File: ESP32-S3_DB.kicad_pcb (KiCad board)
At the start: 2 copper layers, 151 parts, among them CN1 JST_Battery, IC1 SP3071EEN-L/TR, IC2 ATA6561-GAQW-N, J1 TYPE-C-31-M12_13, J10 Conn_01x16_Socket, J11 CAN_TX, J12 CAN_RX, J2 A - B, J3 H - L, J4 TYPE-C-31-M12_13, J5 EXT_LOAD, J6 R4_TX, J7 R4_RX, J8 Micro_SD_Card_Det1, J9 Conn_01x16_Socket, Q1 NMOS, Q2 NMOS, SW1 RESET, SW2 BOOT, SW3 ON/OFF, U1 ESP32-S3FH4R2, U3 IP5306, U4 CH340X, U5 LD1117DT33CTR, X1 32.768KHz, Y1 40MHz

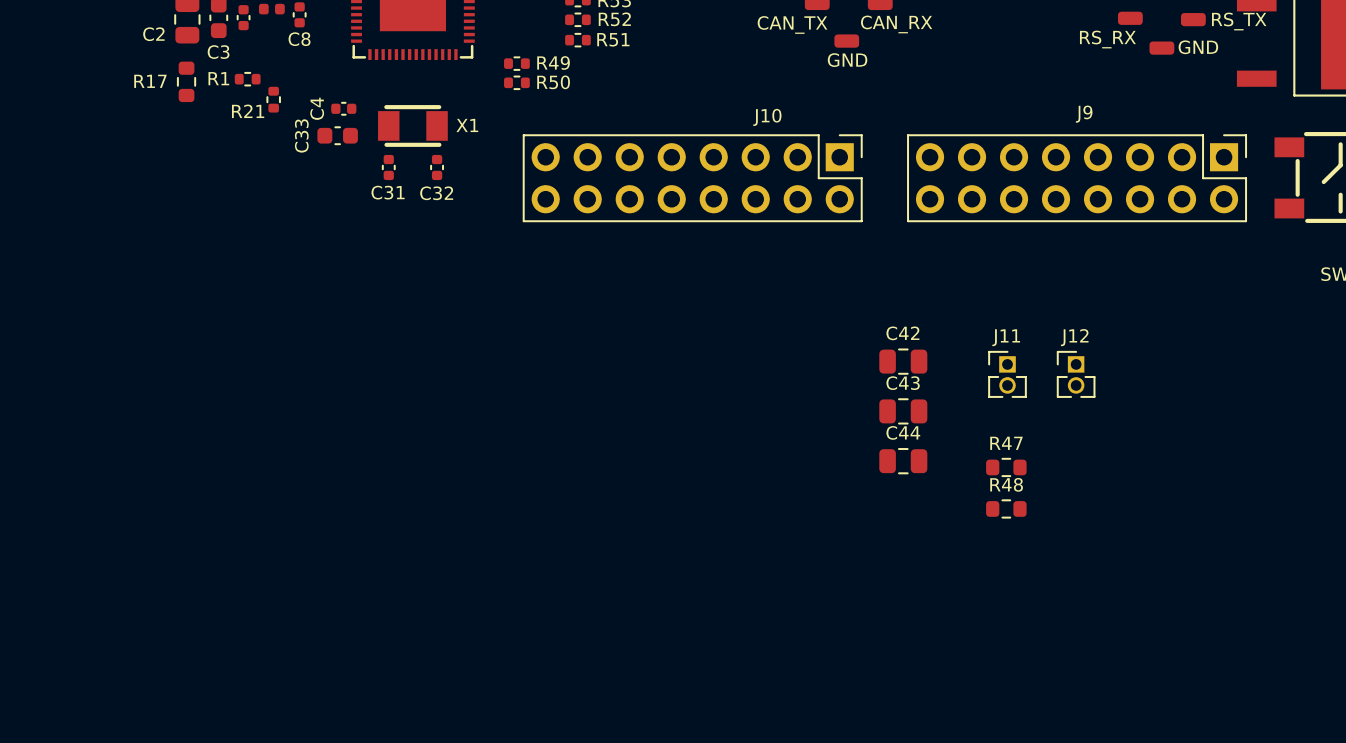
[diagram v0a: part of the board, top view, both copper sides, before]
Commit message: Changed GPIO headers to Arduino style
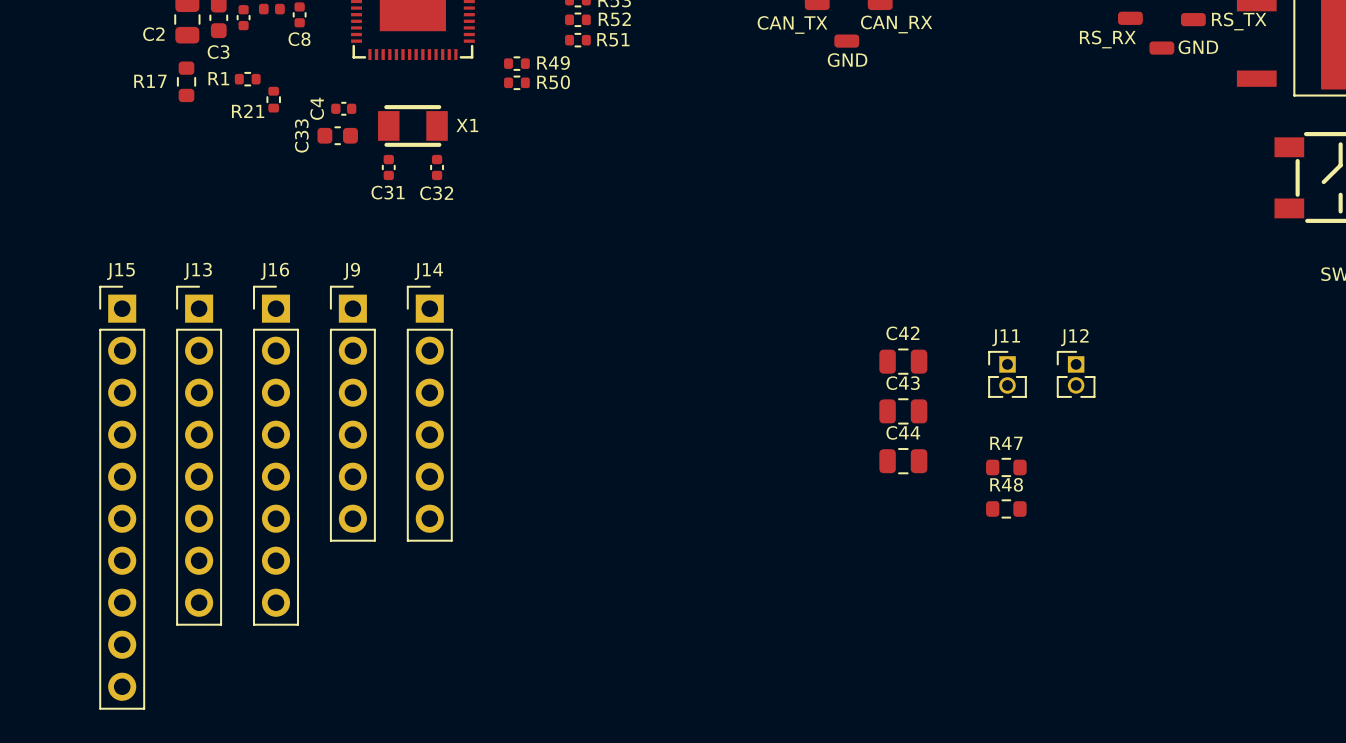
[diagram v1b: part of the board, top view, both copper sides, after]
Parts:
- removed J10: Conn_01x16_Socket, ESP32-S3_Dev_Board:PinHeader_2x08_P2.54mm_Vertical
- added J13: Conn_01x08, ESP32-S3_Dev_Board:PinHeader_1x08_P2.54mm_Vertical, F.Cu at (112.6, 138.7)
- added J14: Conn_01x06, ESP32-S3_Dev_Board:PinHeader_1x06_P2.54mm_Vertical, F.Cu at (126.5, 138.7)
- added J15: Conn_01x10, ESP32-S3_Dev_Board:PinHeader_1x10_P2.54mm_Vertical, F.Cu at (107.9, 138.7)
- added J16: Conn_01x08, ESP32-S3_Dev_Board:PinHeader_1x08_P2.54mm_Vertical, F.Cu at (117.2, 138.7)
- J9: value Conn_01x16_Socket -> Conn_01x06; footprint ESP32-S3_Dev_Board:PinHeader_2x08_P2.54mm_Vertical -> ESP32-S3_Dev_Board:PinHeader_1x06_P2.54mm_Vertical
- moved J9 53.5 mm to (121.9, 138.7), turned to 0 degrees
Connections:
- J9 pad 1: /GPIO14 -> /RS-485_TX/GPIO45
- J9 pad 2: /GPIO9 -> /RS-485_RX/GPIO46
- J9 pad 3: /GPIO6 -> /GPIO40
- J9 pad 4: /GPIO5 -> /GPIO41
- J9 pad 5: /GPIO4 -> /R4_~{RE}_DE
- J9 pad 6: /GPIO3 -> /3V3

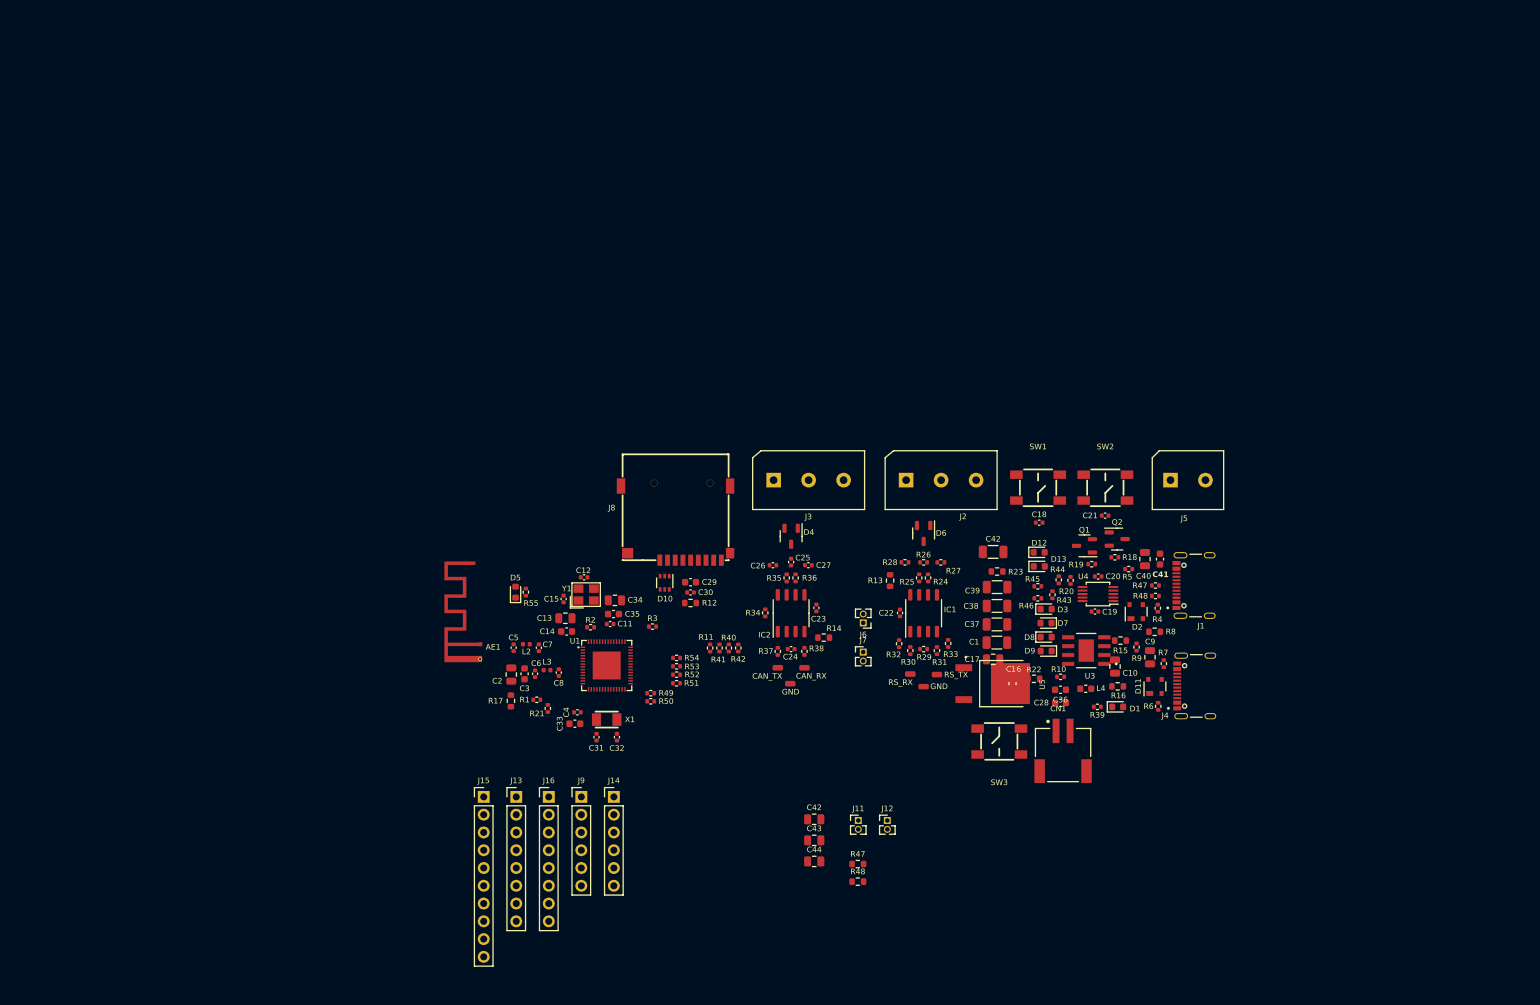
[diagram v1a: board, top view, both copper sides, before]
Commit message: Arranged IP5306, Added support for USB-To-RS485
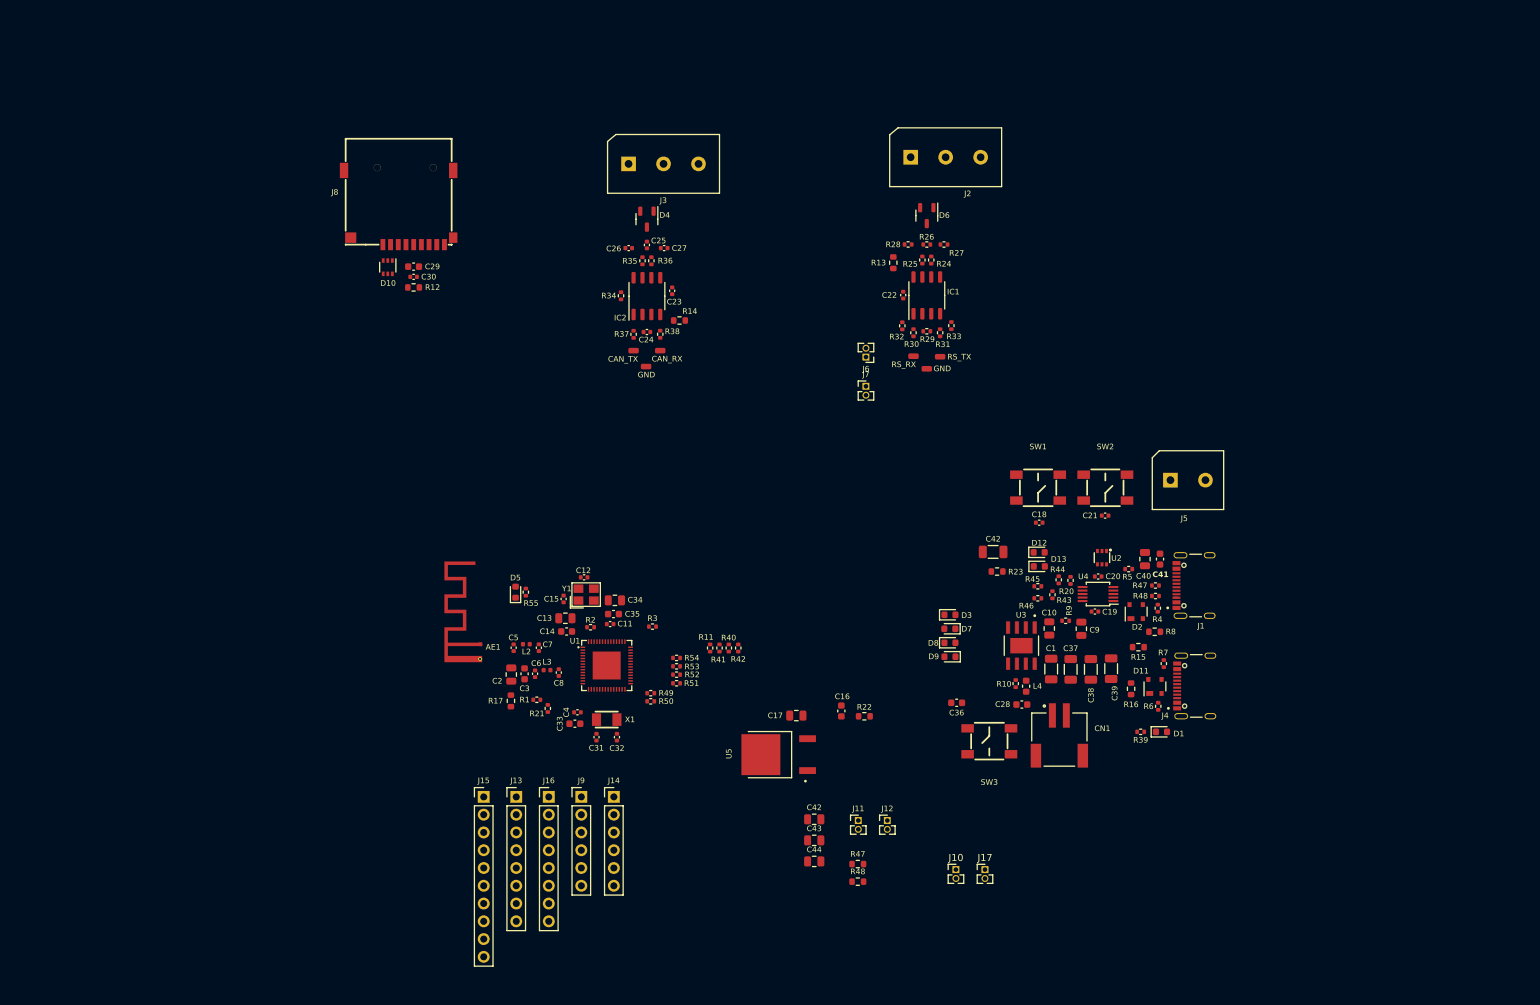
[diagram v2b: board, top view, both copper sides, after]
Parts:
- removed Q1, Q2: NMOS, ESP32-S3_Dev_Board:SOT-23-3
- removed R18, R19: 10k, ESP32-S3_Dev_Board:R_0402_1005Metric
- added J10: U2RS485_TX, ESP32-S3_Dev_Board:PinHeader_1x02_P1.27mm_Vertical, F.Cu at (175.4, 149.1)
- added J17: U2RS485_RX, ESP32-S3_Dev_Board:PinHeader_1x02_P1.27mm_Vertical, F.Cu at (179.6, 149.1)
- added U2: UMH3N, ESP32-S3_Dev_Board:SC-70-6_L2.2-W1.3-P0.65-LS2.1-BR, F.Cu at (196.3, 104.5)
- moved D10 60.0 mm to (94.2, 63.0)
- moved J8 60.0 mm to (95.8, 54.5)
- moved R12 60.0 mm to (97.9, 65.9)
- moved C29 60.0 mm to (97.9, 62.9)
- moved C30 60.0 mm to (97.9, 64.4)
- moved C23 49.8 mm to (134.9, 66.4)
- moved TP6 49.8 mm to (131.1, 77.2)
- moved C24 49.8 mm to (131.2, 72.3)
- moved C25 49.8 mm to (131.2, 59.8)
- moved R37 49.8 mm to (129.3, 72.6)
- moved C26 49.8 mm to (128.6, 60.3)
- moved R36 49.8 mm to (131.9, 62.1)
- moved C27 49.8 mm to (133.7, 60.3)
- moved D4 49.8 mm to (131.2, 56.1)
- moved IC2 49.8 mm to (131.2, 67.1)
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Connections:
- net /U2U_RXD renamed /485_U2U_RX
- net Net-(U4-TXD) renamed /485_U2U_TX
- C1 pad 1: /5V -> Net-(U3-VOUT)
- C37 pad 1: /5V -> Net-(U3-VOUT)
- C38 pad 1: /5V -> Net-(U3-VOUT)
- C39 pad 1: /5V -> Net-(U3-VOUT)
- R20 pad 2: /USB-TO-UART/DTR -> /R4_~{RE}_DE
- R9 pad 1: /INPUT POWER/VIN -> Net-(U3-VIN)
- U4 pad 6: /USB-TO-UART/DTR -> /R4_~{RE}_DE

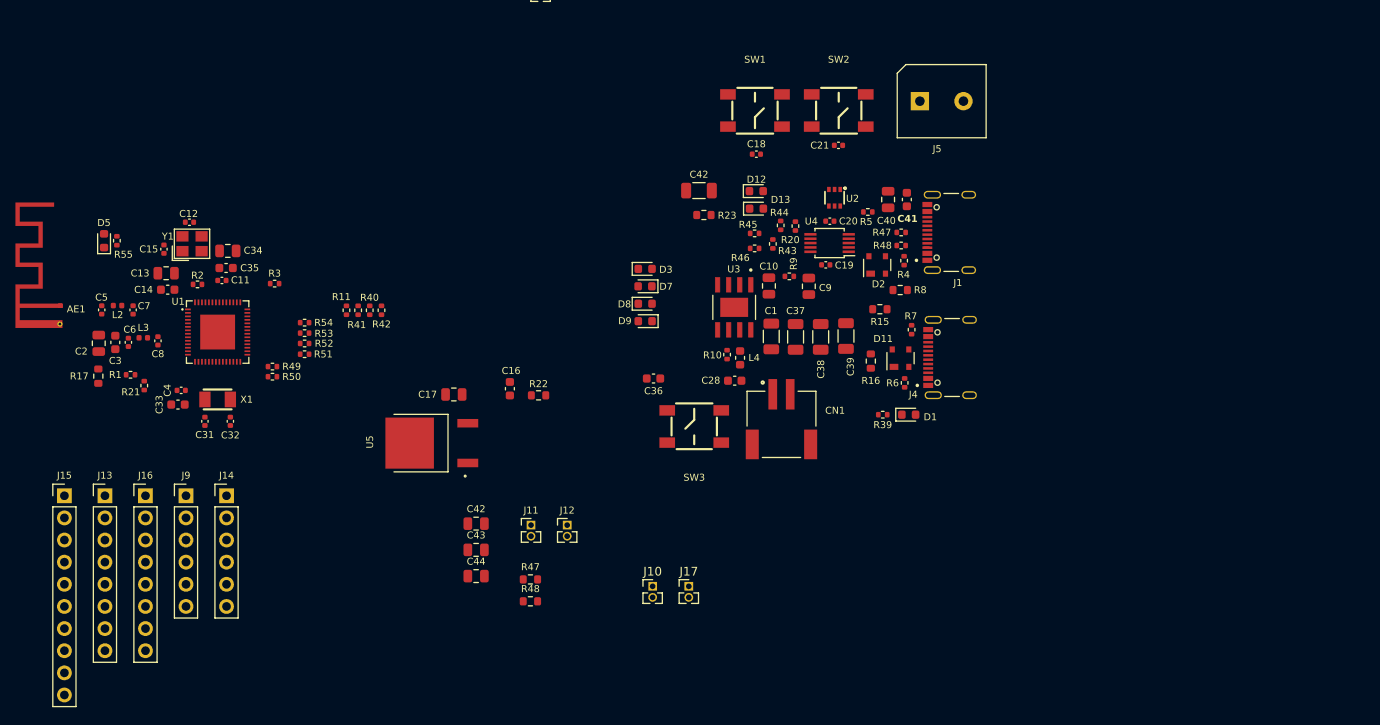
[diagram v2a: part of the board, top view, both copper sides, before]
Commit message: Arranged arduino headers as per the Uno R3 dimensions
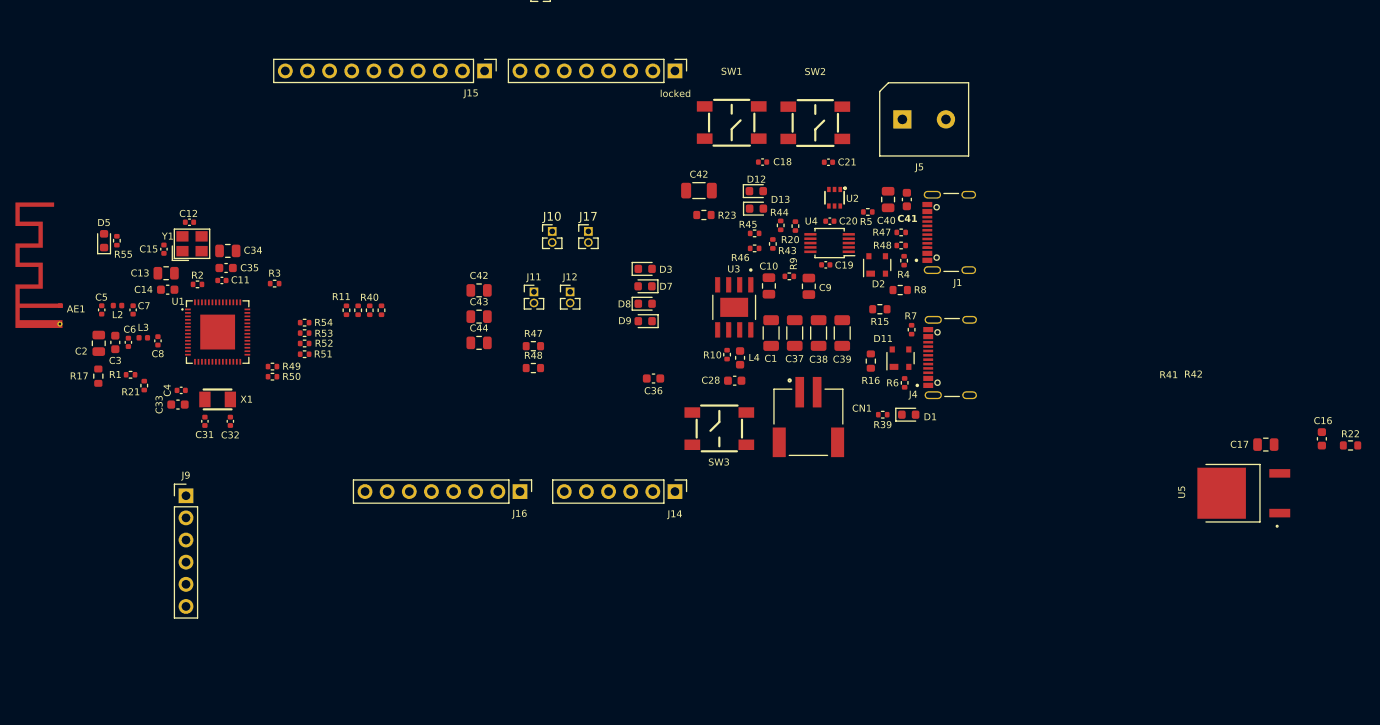
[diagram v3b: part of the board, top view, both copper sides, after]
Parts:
- moved C16 93.3 mm to (252.2, 132.2)
- moved C17 93.3 mm to (245.8, 132.8)
- moved R22 93.3 mm to (255.5, 132.9)
- moved U5 93.3 mm to (243.2, 138.4)
- moved locked 81.6 mm to (178.0, 90.0), turned to -90 degrees
- moved J15 68.6 mm to (156.1, 90.0), turned to -90 degrees
- moved J14 51.5 mm to (178.0, 138.2), turned to -90 degrees
- moved J16 43.0 mm to (160.2, 138.2), turned to -90 degrees
- moved J10 42.3 mm to (163.9, 108.4)
- moved J17 42.3 mm to (168.0, 108.4)
- moved J11 26.8 mm to (161.8, 115.3)
- moved J12 26.8 mm to (165.9, 115.3)
- moved C44 26.8 mm to (155.5, 121.2)
- moved R47 26.8 mm to (161.7, 121.5)
- moved C42 26.8 mm to (155.5, 115.2)
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- renumbered J13 to locked
